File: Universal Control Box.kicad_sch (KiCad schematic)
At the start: 22 parts, among them J101 Conn_01x06, J102 Conn_01x07, J103 USB_C_Receptacle_USB2.0, U101 ESP32-WROOM-32, U102 PCF8575DBR (PCF1), U103 AMS1117-3.3

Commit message: Made changes based on Josh's comments & switched to Switched to WS2812B-2020
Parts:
- removed U103: AMS1117-3.3, Package_TO_SOT_SMD:SOT-223-3_TabPin2, symbol Regulator_Linear:AMS1117-3.3
- added U103: XC6220B331MR-G, Package_TO_SOT_SMD:SOT-23-5, symbol Regulator_Linear:XC6220B331MR
- C104: value 10uF -> 22uF; LCSC C96446 -> C59461
- C105: value 10uF -> 4.7uF; LCSC C96446 -> C19666
- U101: footprint Josh_Custom_Footprints:ESP32-WROOM-32 -> RF_Module:ESP32-WROOM-32
- U102: footprint Adam_Custom_Footprints:TexasInstruments_PCF8575DBR -> DB24
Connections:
- net +3.3V: now also U103.5 (VOUT)
- net +5V: now also C104.2, U103.1 (VIN), U103.3 (CE); no longer C104.1
- net GND: now also C104.1, U103.2 (GND); no longer C104.2
- net KeyCaps/SW10: now also U102.10 (P06); no longer U102.19 (P16)
- net KeyCaps/SW11: now also U102.9 (P05); no longer U102.18 (P15)
- net KeyCaps/SW12: now also U102.8 (P04); no longer U102.17 (P14)
- net KeyCaps/SW13: now also U102.13 (P10); no longer U102.16 (P13)
- net KeyCaps/SW14: now also U102.14 (P11); no longer U102.15 (P12)
- net KeyCaps/SW15: now also U102.15 (P12); no longer U102.14 (P11)
- net KeyCaps/SW16: now also U102.16 (P13); no longer U102.13 (P10)
- net KeyCaps/SW5: now also U102.20 (P17); no longer U102.8 (P04)
- net KeyCaps/SW6: now also U102.19 (P16); no longer U102.9 (P05)
- net KeyCaps/SW7: now also U102.18 (P15); no longer U102.10 (P06)
- net KeyCaps/SW8: now also U102.17 (P14); no longer U102.11 (P07)
- net KeyCaps/SW9: now also U102.11 (P07); no longer U102.20 (P17)
- net IO_INT: now reaches U102.1 (*INT)
- net IO_INT: now also U101.31 (IO19)
- no-connect marks 22 -> 20
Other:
- moved on the sheet: J102

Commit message: Fixed LED Schematic & added 2 more LEDs
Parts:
- removed R101: 1K, Resistor_SMD:R_0603_1608Metric, symbol Device:R_Small
- added D102: Green, LED_SMD:LED_0603_1608Metric, symbol Device:LED
- added D103: Yellow, LED_SMD:LED_0603_1608Metric, symbol Device:LED
- added R104, R105: 1K, Resistor_SMD:R_0603_1608Metric, symbol Device:R_Small
- U101: footprint RF_Module:ESP32-WROOM-32 -> Josh_Custom_Footprints:ESP32-WROOM-32
- U102: footprint DB24 -> Adam_Custom_Footprints:TexasInstruments_PCF8575DBR
- renumbered R102 to R101, R103 to R102, R104 to R103
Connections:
- net +3.3V: now also R104.2, R105.2; no longer D101.2 (A)
- net ESP_TX: now also D103.1 (K)
- net GND: now also D101.1 (K), D102.1 (K)
- net KeyCaps/SW13: now also U102.16 (P13); no longer U102.13 (P10)
- net KeyCaps/SW14: now also U102.15 (P12); no longer U102.14 (P11)
- net KeyCaps/SW15: now also U102.14 (P11); no longer U102.15 (P12)
- net KeyCaps/SW16: now also U102.13 (P10); no longer U102.16 (P13)
- net KeyCaps/SW5: now also U102.17 (P14); no longer U102.20 (P17)
- net KeyCaps/SW6: now also U102.18 (P15); no longer U102.19 (P16)
- net KeyCaps/SW7: now also U102.19 (P16); no longer U102.18 (P15)
- net KeyCaps/SW8: now also U102.20 (P17); no longer U102.17 (P14)
- net HA_STATUS: now reaches U101.23 (IO15)
- net HA_STATUS: now also D102.2 (A)
- new net: D101.2 (A), R104.1
- new net: D103.2 (A), R105.1
- no-connect marks 20 -> 19
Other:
- moved on the sheet: D101, H101, H102, H103, H104

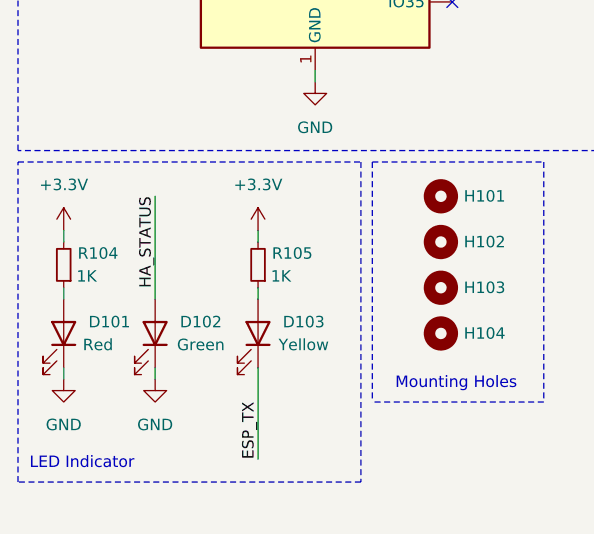
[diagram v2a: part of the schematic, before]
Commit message: Added missing resistor for Green LED
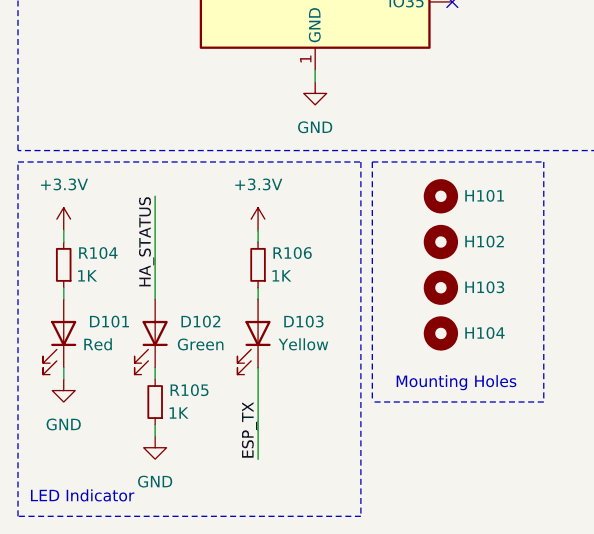
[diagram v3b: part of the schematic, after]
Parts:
- added R106: 1K, Resistor_SMD:R_0603_1608Metric, symbol Device:R_Small
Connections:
- net +3.3V: now also R106.2; no longer R105.2
- net GND: now also R105.1; no longer D102.1 (K)
- net at D103.2 (A): now also R106.1; no longer R105.1
- new net: D102.1 (K), R105.2
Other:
- moved on the sheet: R105
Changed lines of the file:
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@@
+    (stroke (width 0) (type default))
+  )
+  (wire (pts (xy 40.64 132.08) (xy 40.64 133.35))
     (stroke (width 0) (type default))
   )
@@
   )
   (wire (pts (xy 62.23 66.04) (xy 82.55 66.04))
+    (stroke (width 0) (type default))
+  )
+  (wire (pts (xy 40.64 138.43) (xy 40.64 139.7))
     (stroke (width 0) (type default))
   )
@@
     (stroke (width 0) (type default))
   )
+  (wire (pts (xy 29.21 147.32) (xy 29.21 148.59))
+    (stroke (width 0) (type default))
+  )
   (wire (pts (xy 29.21 128.27) (xy 29.21 139.7))
     (stroke (width 0) (type default))
@@
     (stroke (width 0) (type default))
   )
-  (wire (pts (xy 40.64 132.08) (xy 40.64 133.35))
-    (stroke (width 0) (type default))
-  )
   (wire (pts (xy 193.04 39.37) (xy 184.15 39.37))
     (stroke (width 0) (type default))
@@
     (stroke (width 0) (type default))
   )
-  (wire (pts (xy 29.21 147.32) (xy 29.21 148.59))
+  (wire (pts (xy 29.21 153.67) (xy 29.21 154.94))
     (stroke (width 0) (type default))
   )
@@
   )
   (wire (pts (xy 46.99 31.75) (xy 52.07 31.75))
-    (stroke (width 0) (type default))
-  )
-  (wire (pts (xy 40.64 138.43) (xy 40.64 139.7))
     (stroke (width 0) (type default))
   )
@@
     (stroke (width 0) (type default))
   )
-  (rectangle (start 13.97 124.46) (end 52.07 160.02)
+  (rectangle (start 13.97 124.46) (end 52.07 163.83)
     (stroke (width 0) (type dash))
     (fill (type none))
@@
     (effects (font (size 1.27 1.27) (color 255 0 255 1)) (justify left bottom))
   )
-  (text "LED Indicator" (at 15.24 158.75 0)
+  (text "LED Indicator" (at 15.24 162.56 0)
     (effects (font (size 1.27 1.27) (color 255 153 0 1)) (justify left bottom))
   )
@@
     )
   )
-  (symbol (lib_id "power:GND") (at 29.21 148.59 0) (unit 1)
-    (in_bom yes) (on_board yes) (dnp no) (fields_autoplaced)
-    (property "Reference" "#PWR0124" (at 29.21 154.94 0)
-      (effects (font (size 1.27 1.27)) hide)
-    )
-    (property "Value" "GND" (at 29.21 153.67 0)
-      (effects (font (size 1.27 1.27)))
-    )
-    (property "Footprint" "" (at 29.21 148.59 0)
-      (effects (font (size 1.27 1.27)) hide)
-    )
-    (property "Datasheet" "" (at 29.21 148.59 0)
+  (symbol (lib_id "power:GND") (at 29.21 154.94 0) (unit 1)
+    (in_bom yes) (on_board yes) (dnp no) (fields_autoplaced)
+    (property "Reference" "#PWR0124" (at 29.21 161.29 0)
+      (effects (font (size 1.27 1.27)) hide)
+    )
+    (property "Value" "GND" (at 29.21 160.02 0)
+      (effects (font (size 1.27 1.27)))
+    )
+    (property "Footprint" "" (at 29.21 154.94 0)
+      (effects (font (size 1.27 1.27)) hide)
+    )
+    (property "Datasheet" "" (at 29.21 154.94 0)
       (effects (font (size 1.27 1.27)) hide)
     )
@@
     )
   )
+  (symbol (lib_id "Device:R_Small") (at 40.64 135.89 180) (unit 1)
+    (in_bom yes) (on_board yes) (dnp no)
+    (property "Reference" "R106" (at 44.45 134.62 0)
+      (effects (font (size 1.27 1.27)))
+    )
+    (property "Value" "1K" (at 43.18 137.16 0)
+      (effects (font (size 1.27 1.27)))
+    )
+    (property "Footprint" "Resistor_SMD:R_0603_1608Metric" (at 42.418 135.89 90)
+      (effects (font (size 1.27 1.27)) hide)
+    )
+    (property "Datasheet" "~" (at 40.64 135.89 0)
+      (effects (font (size 1.27 1.27)) hide)
+    )
+    (property "LCSC" "C21190" (at 40.64 135.89 0)
+      (effects (font (size 1.27 1.27)) hide)
+    )
+    (pin "1")
+    (pin "2")
+    (instances
+      (project "Universal Control Box"
+        (path "/0356e092-4721-4291-8799-df5160707ecc"
+          (reference "R106") (unit 1)
+        )
+      )
+    )
+  )
   (symbol (lib_id "Device:C_Small") (at 137.16 121.92 0) (mirror x) (unit 1)
     (in_bom yes) (on_board yes) (dnp no) (fields_autoplaced)
@@
     )
   )
-  (symbol (lib_id "Device:R_Small") (at 40.64 135.89 180) (unit 1)
+  (symbol (lib_id "Device:R_Small") (at 29.21 151.13 180) (unit 1)
     (in_bom yes) (on_board yes) (dnp no)
-    (property "Reference" "R105" (at 44.45 134.62 0)
-      (effects (font (size 1.27 1.27)))
-    )
-    (property "Value" "1K" (at 43.18 137.16 0)
-      (effects (font (size 1.27 1.27)))
-    )
-    (property "Footprint" "Resistor_SMD:R_0603_1608Metric" (at 42.418 135.89 90)
-      (effects (font (size 1.27 1.27)) hide)
-    )
-    (property "Datasheet" "~" (at 40.64 135.89 0)
-      (effects (font (size 1.27 1.27)) hide)
-    )
-    (property "LCSC" "C21190" (at 40.64 135.89 0)
-      (effects (font (size 1.27 1.27)) hide)
-    )
+    (property "Reference" "R105" (at 33.02 149.86 0)
+      (effects (font (size 1.27 1.27)))
+    )
+    (property "Value" "1K" (at 31.75 152.4 0)
+      (effects (font (size 1.27 1.27)))
+    )
+    (property "Footprint" "Resistor_SMD:R_0603_1608Metric" (at 30.988 151.13 90)
+      (effects (font (size 1.27 1.27)) hide)
+    )
+    (property "Datasheet" "~" (at 29.21 151.13 0)
+      (effects (font (size 1.27 1.27)) hide)
+    )
+    (property "LCSC" "C21190" (at 29.21 151.13 0)
+      (effects (font (size 1.27 1.27)) hide)
+    )

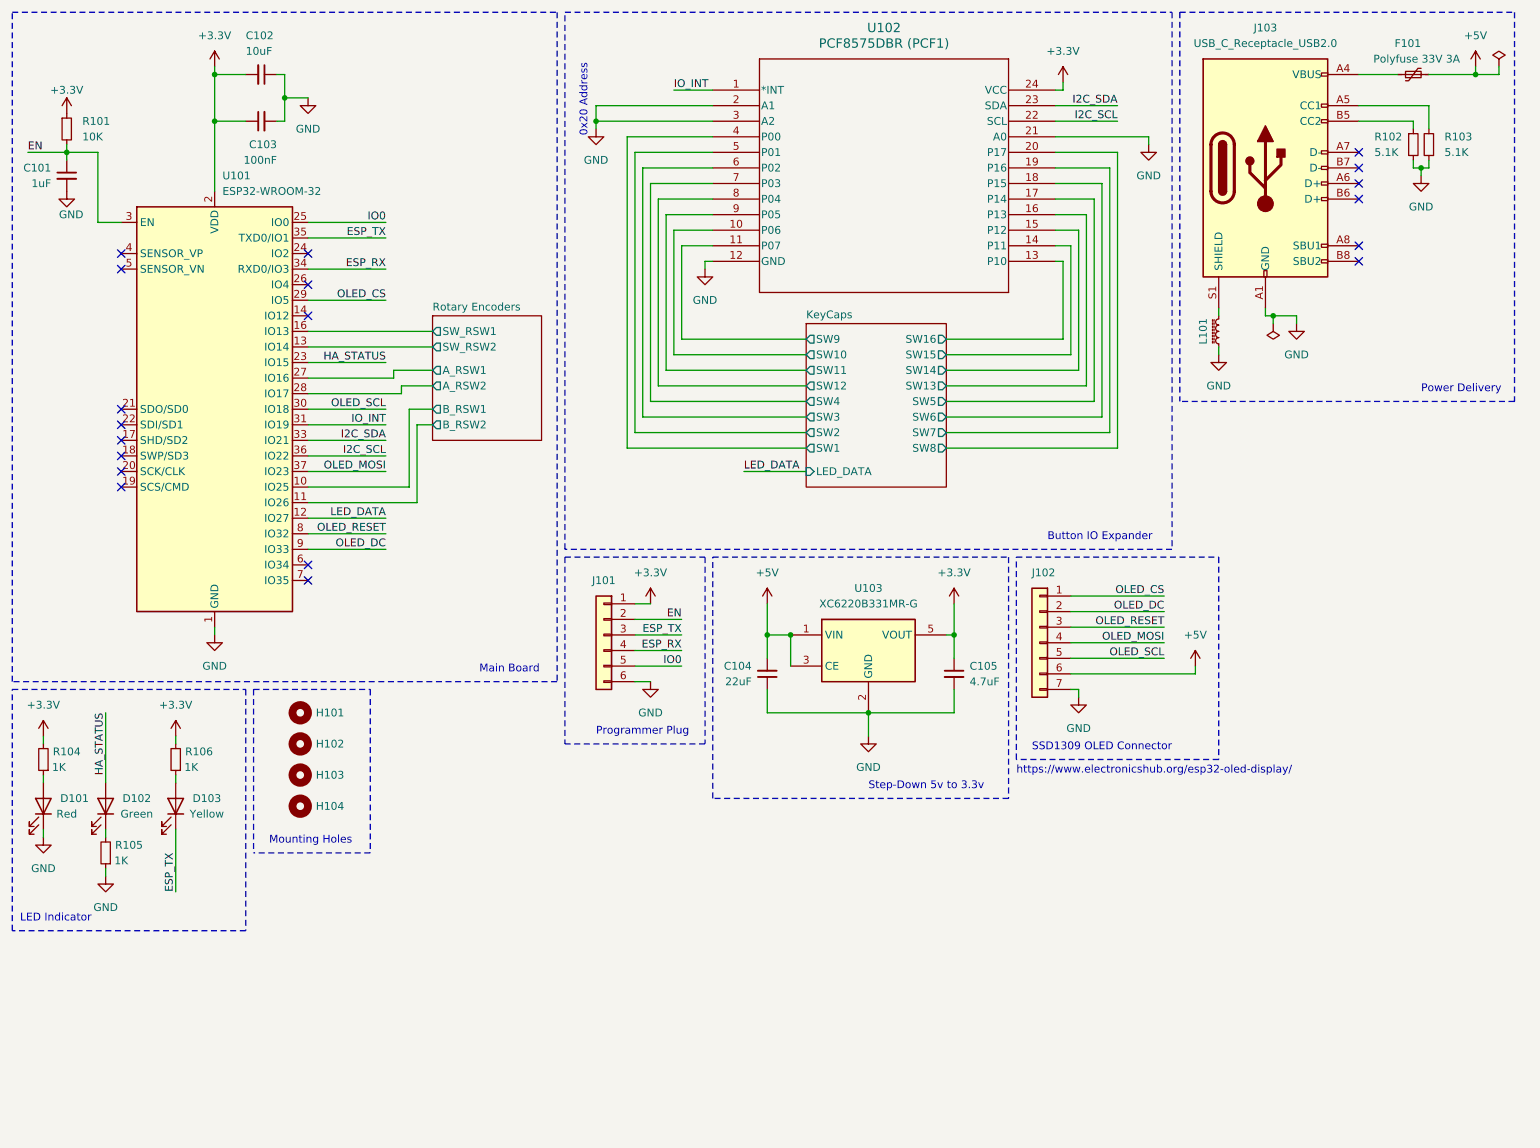
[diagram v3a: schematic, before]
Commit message: Added GND & other stuff
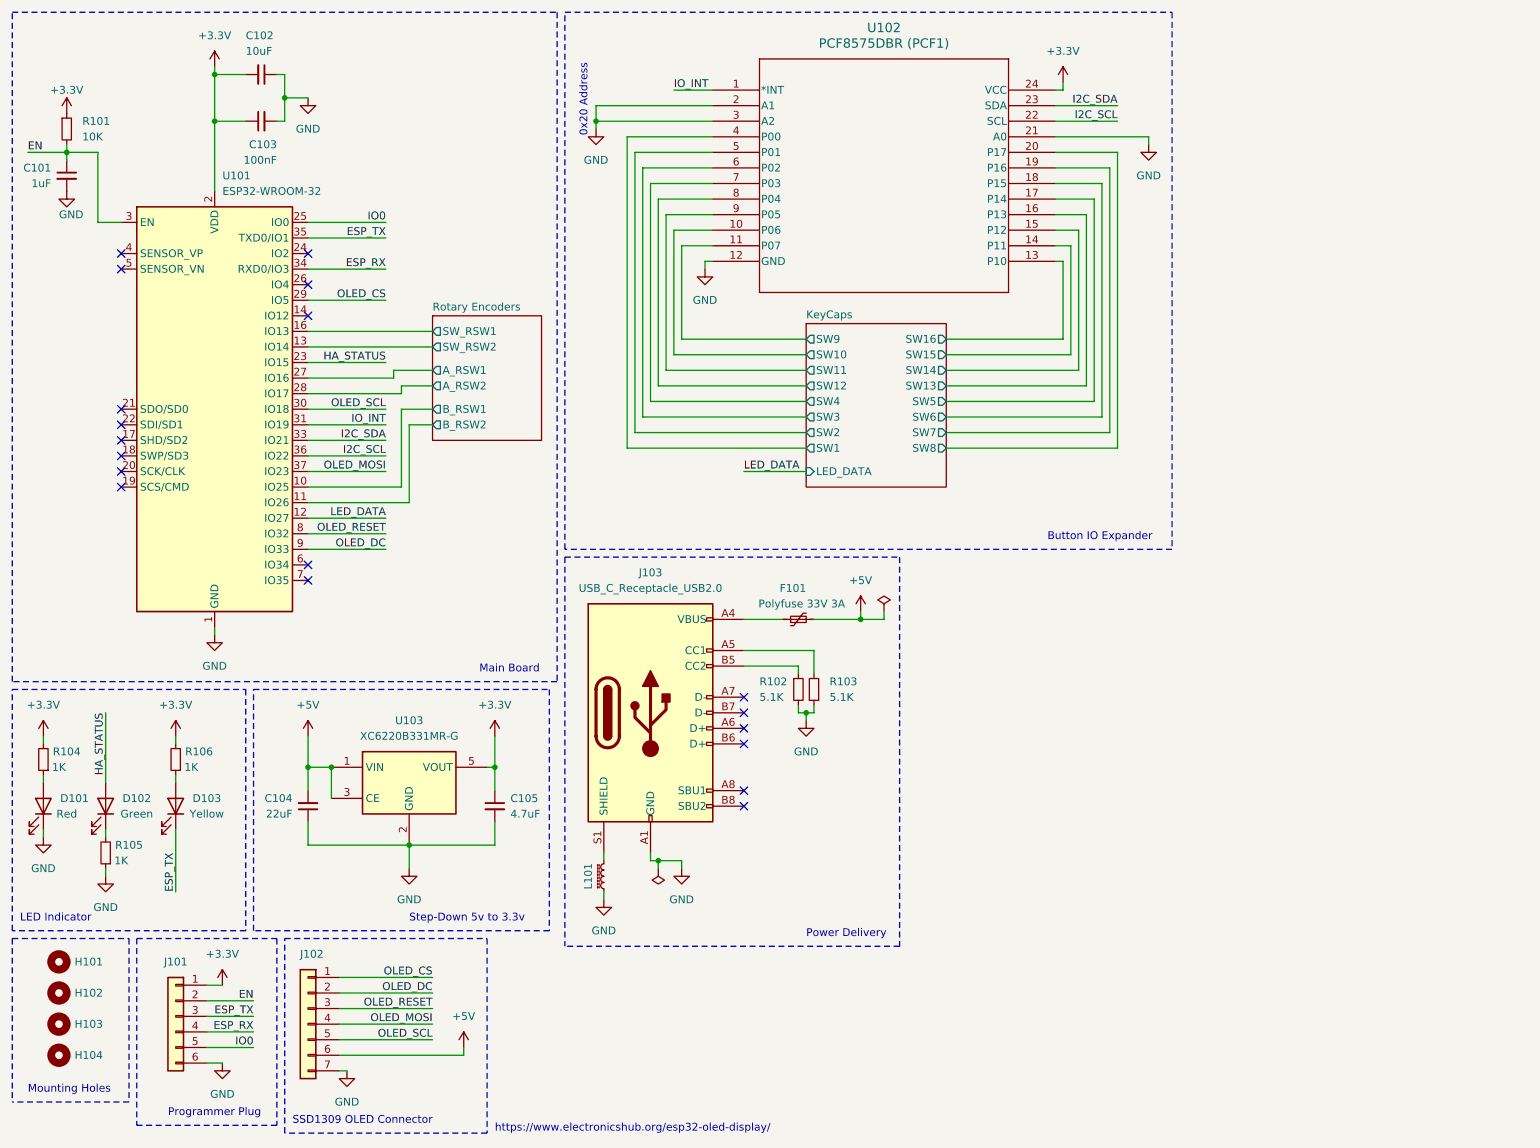
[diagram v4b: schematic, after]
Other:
- moved on the sheet: C104, C105, F101, H101, H102, H103, H104, J101, J102, J103, L101, R102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
